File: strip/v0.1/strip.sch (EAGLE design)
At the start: 100 parts, among them IC1 LP2992, IC11 AP1115BY50, IC2 ADP3110A-SO8, IC3 STM32-M-48, IC4 OPA335, IC5 ADP3110A-SO8, IC6 ADP3110A-SO8, Q1 IRF7828, Q2 IRF7828, Q3 IRF7828, Q4 IRF7828, Q5 IRF7828, Q6 IRF7828

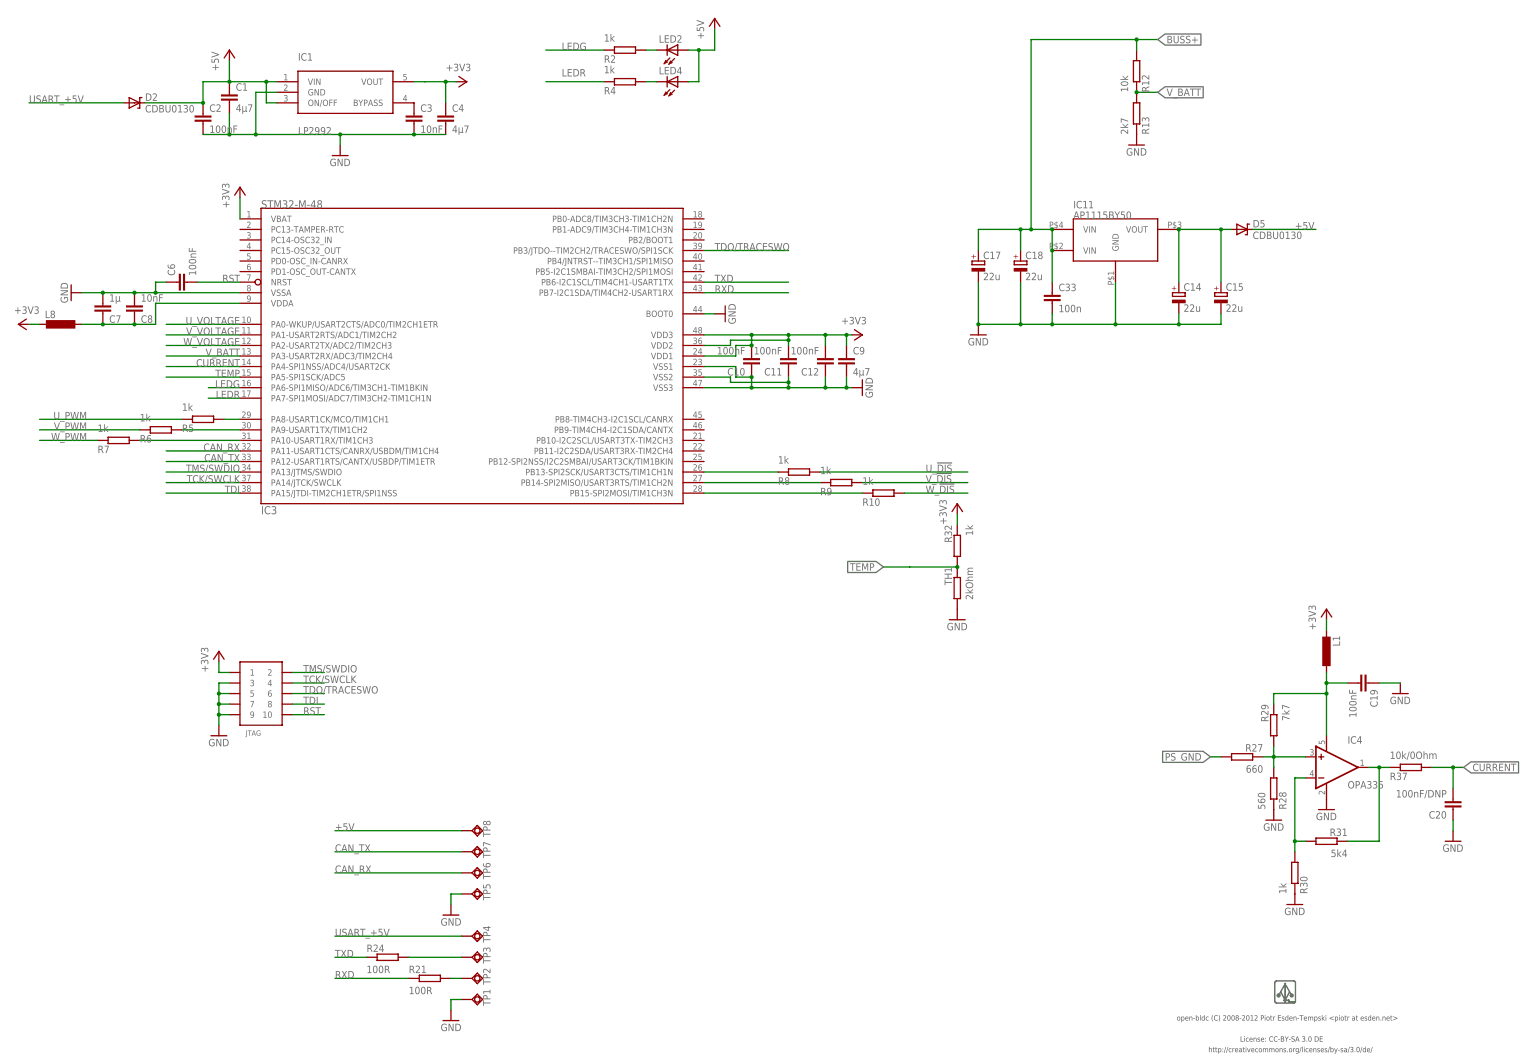
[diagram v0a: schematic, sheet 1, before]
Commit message: More work on strip. Preliminary routing of the power stage.
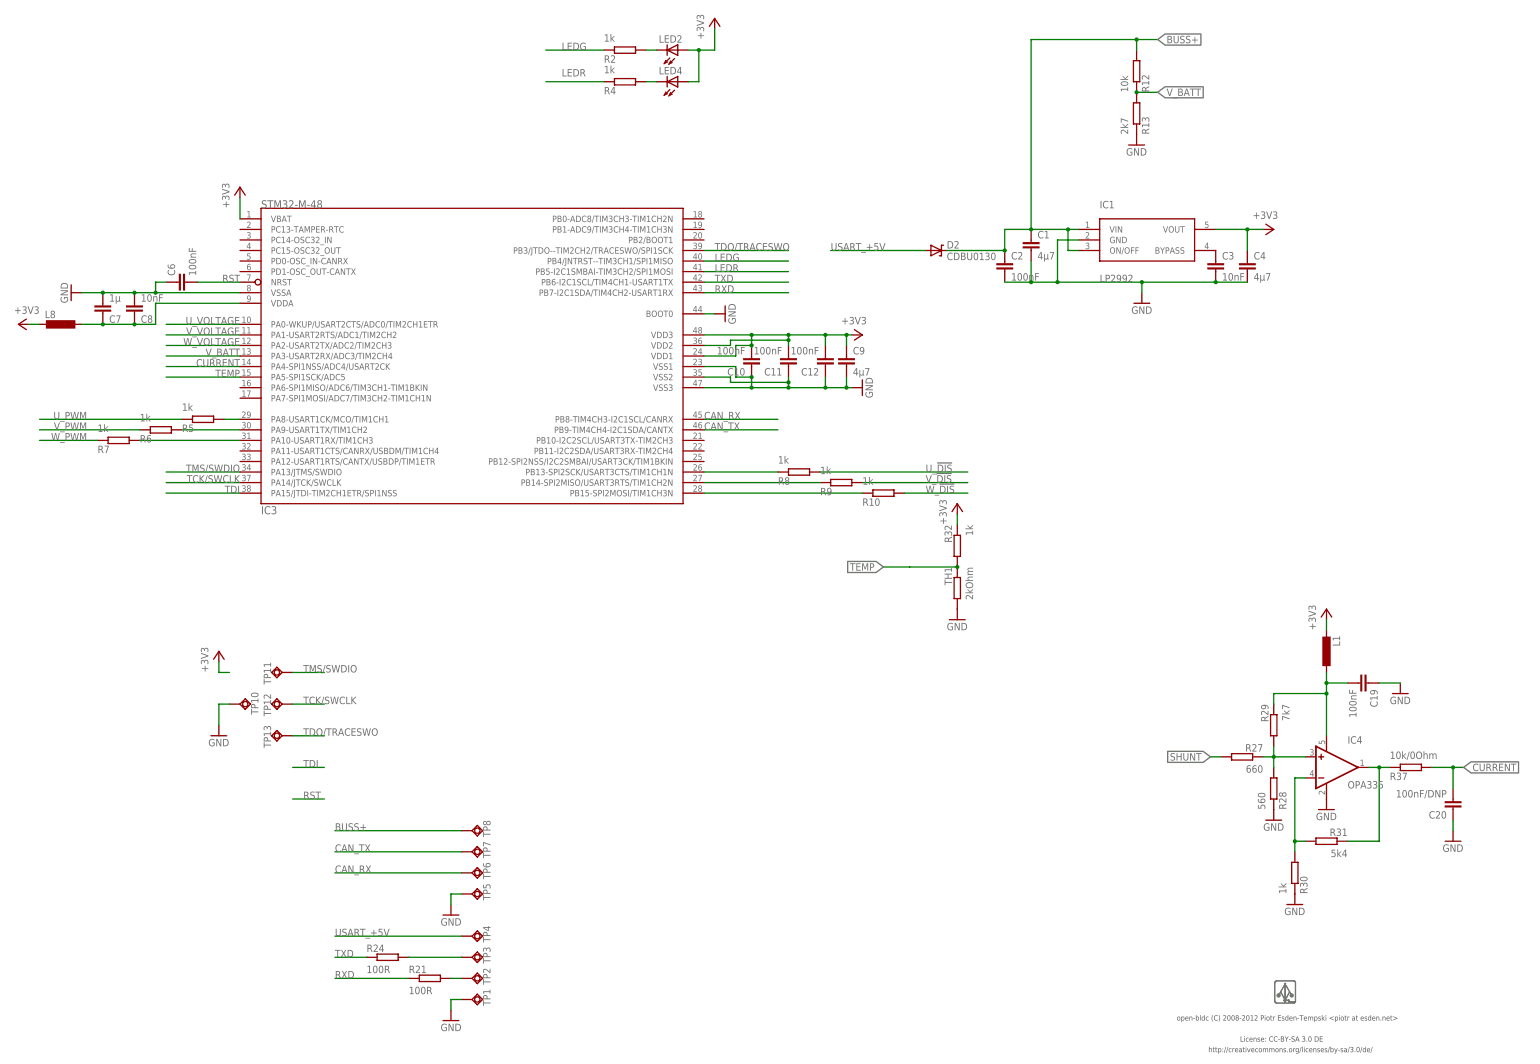
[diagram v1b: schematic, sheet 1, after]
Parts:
- removed C14, C15, C17, C18: 22u, pel_dipol_comp:CAPACITOR-POL-0805
- removed C33: 100n, pel_dipol_comp:CAPACITOR-0402
- removed D5: CDBU0130, pel_dipol_comp:DIODE-ZENER-0603
- removed IC11: AP1115BY50, clogic-v0_3-r1:AP1115BY50
- removed JTAG: CONN_5-2-FTSH-V, pel_misc:CONN_5-2-FTSH-V
- added TP10, TP11, TP12, TP13: TPSQTP11SQ, testpad:TPSQTP11SQ
- C11: device pel_dipol_comp:CAPACITOR-0603 -> pel_dipol_comp:CAPACITOR-0402
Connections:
- removed net +5V: C1.1, C2.1, D2.C, D5.C, IC1.ON/OFF, IC1.VIN, LED2.A, LED4.A, TP8.TP
- removed net +5VOUT: C14.+, C15.+, D5.A, IC11.VOUT
- removed net PS_GND: IC2.PGND, IC5.PGND, IC6.PGND, Q2.S1, Q2.S2, Q2.S3, Q4.S1, Q4.S2, Q4.S3, Q6.S1, Q6.S2, Q6.S3, R27.2, R45.1
- new net SHUNT: PAD4.P, R27.2, R45.2
- net +3V3: now also LED2.A, LED4.A; no longer JTAG.1
- net BUSS+: now also C1.1, C2.1, D2.C, IC1.ON/OFF, IC1.VIN, TP8.TP; no longer C17.+, C18.+, C33.1, IC11.VIN, IC11.VIN@2
- net CAN_RX: now also IC3.PB8-TIM4CH3-I2C1SCL/CANRX; no longer IC3.PA11-USART1CTS/CANRX/USBDM/TIM1CH4
- net CAN_TX: now also IC3.PB9-TIM4CH4-I2C1SDA/CANTX; no longer IC3.PA12-USART1RTS/CANTX/USBDP/TIM1ETR
- net GND: now also IC2.PGND, IC5.PGND, IC6.PGND, Q2.S1, Q2.S2, Q2.S3, Q4.S1, Q4.S2, Q4.S3, Q6.S1, Q6.S2, Q6.S3, R45.1, TP10.TP; no longer C14.-, C15.-, C17.-, C18.-, C33.2, IC11.GND, JTAG.3, JTAG.5, JTAG.7, JTAG.9, PAD4.P, R45.2
- net LEDG: now also IC3.PB4/JNTRST--TIM3CH1/SPI1MISO; no longer IC3.PA6-SPI1MISO/ADC6/TIM3CH1-TIM1BKIN
- net LEDR: now also IC3.PB5-I2C1SMBAI-TIM3CH2/SPI1MOSI; no longer IC3.PA7-SPI1MOSI/ADC7/TIM3CH2-TIM1CH1N
- net RST: no longer JTAG.10
- net TCK/SWCLK: now also TP12.TP; no longer JTAG.4
- net TDI: no longer JTAG.8
- net TDO/TRACESWO: now also TP13.TP; no longer JTAG.6
- net TMS/SWDIO: now also TP11.TP; no longer JTAG.2
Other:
- moved on the sheet: C1, C2, C3, C4, D2, IC1

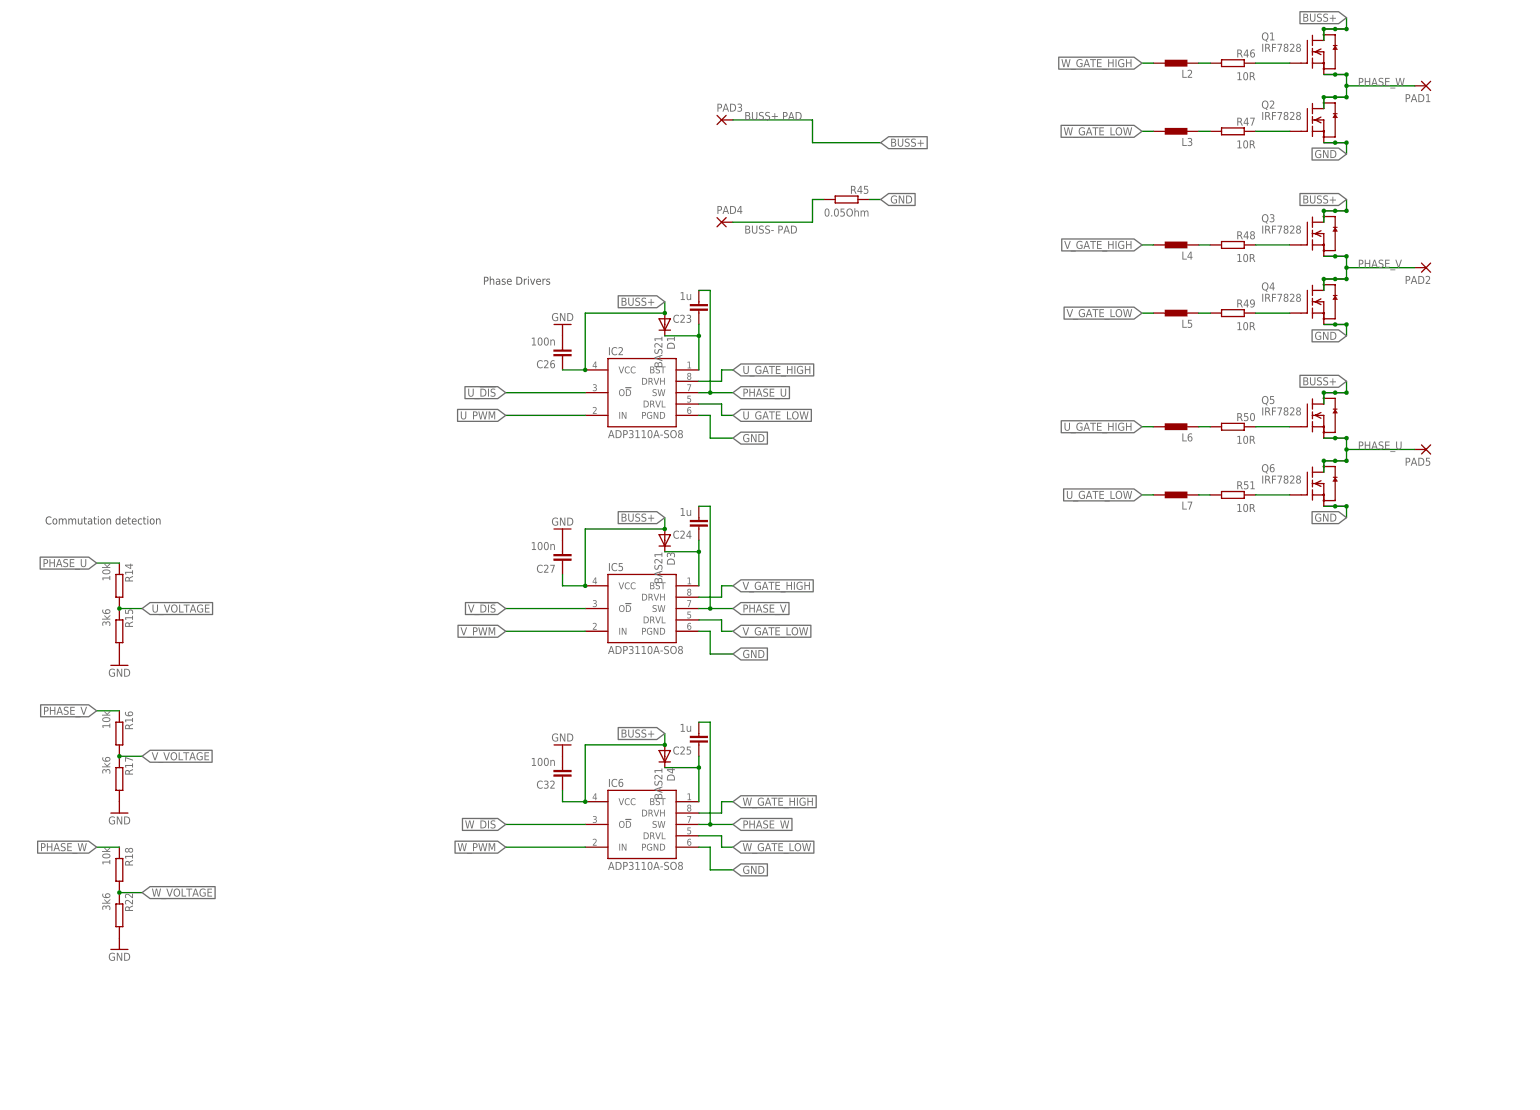
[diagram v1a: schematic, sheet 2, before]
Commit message: Logic is on real GND now not pstage GND, to prevent current related logic signal bouncing. Added mounting holes.
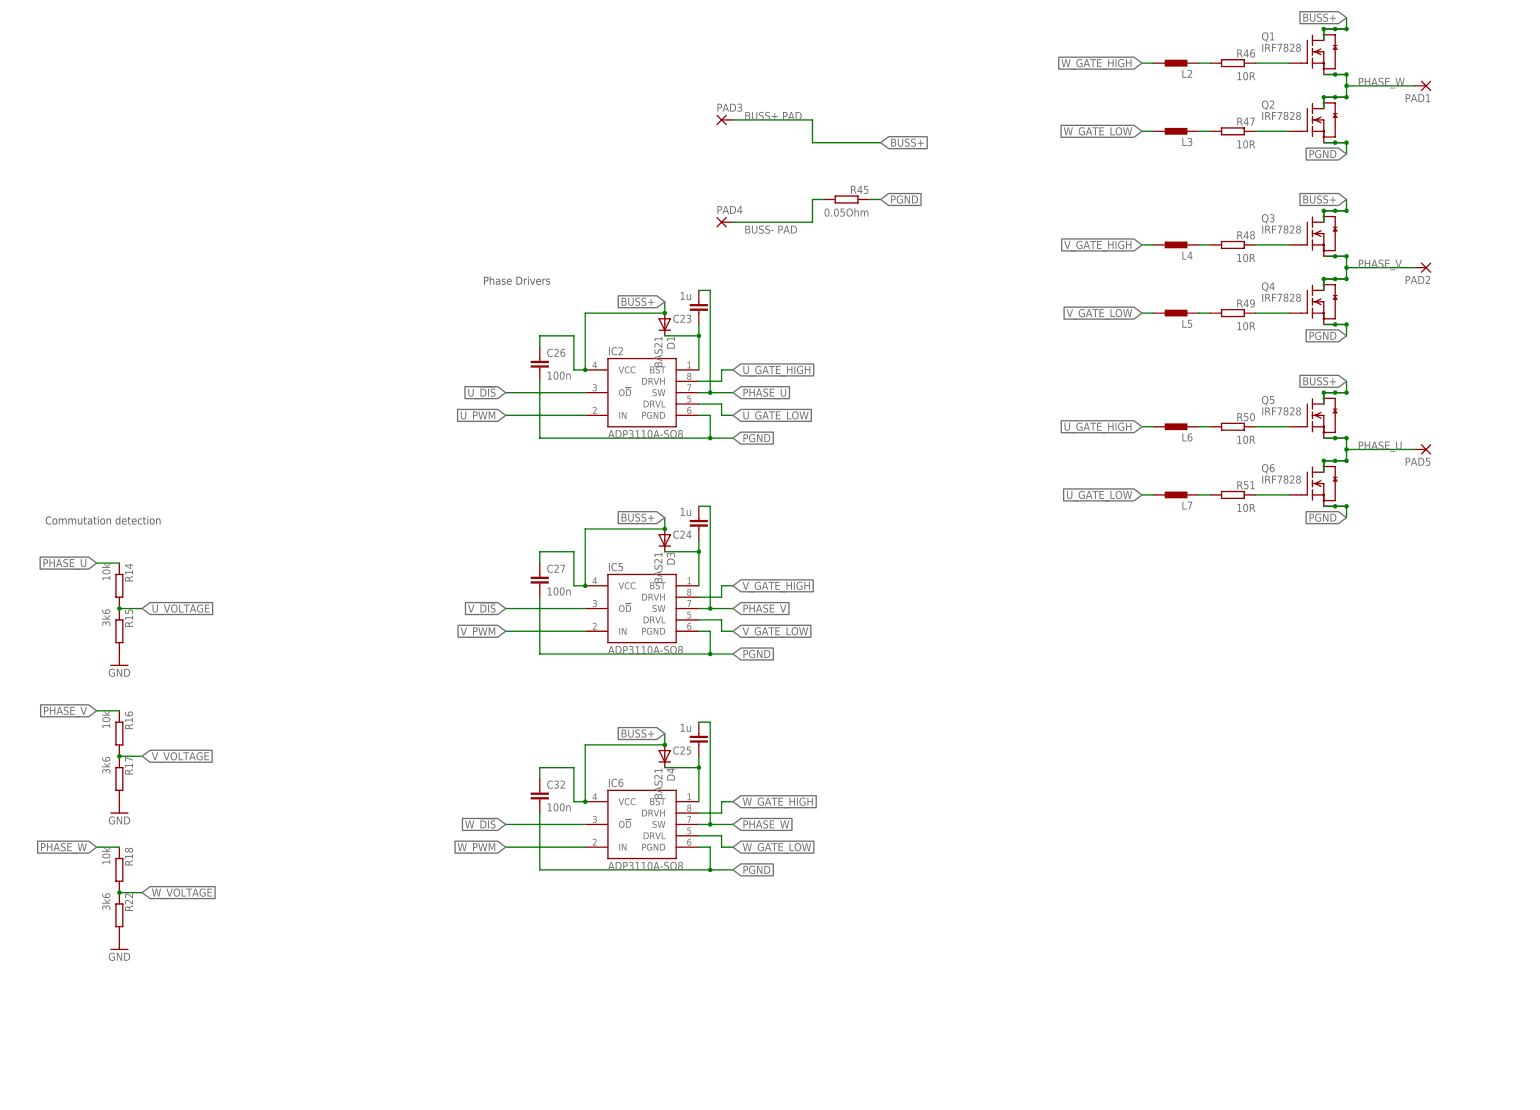
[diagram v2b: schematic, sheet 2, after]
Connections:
- removed net SHUNT: PAD4.P, R27.2, R45.2
- new net PGND: C26.2, C27.2, C32.2, IC2.PGND, IC5.PGND, IC6.PGND, Q2.S1, Q2.S2, Q2.S3, Q4.S1, Q4.S2, Q4.S3, Q6.S1, Q6.S2, Q6.S3, R27.2, R45.1
- net GND: now also PAD4.P, R45.2; no longer C26.2, C27.2, C32.2, IC2.PGND, IC5.PGND, IC6.PGND, Q2.S1, Q2.S2, Q2.S3, Q4.S1, Q4.S2, Q4.S3, Q6.S1, Q6.S2, Q6.S3, R45.1
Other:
- moved on the sheet: C26, C27, C32

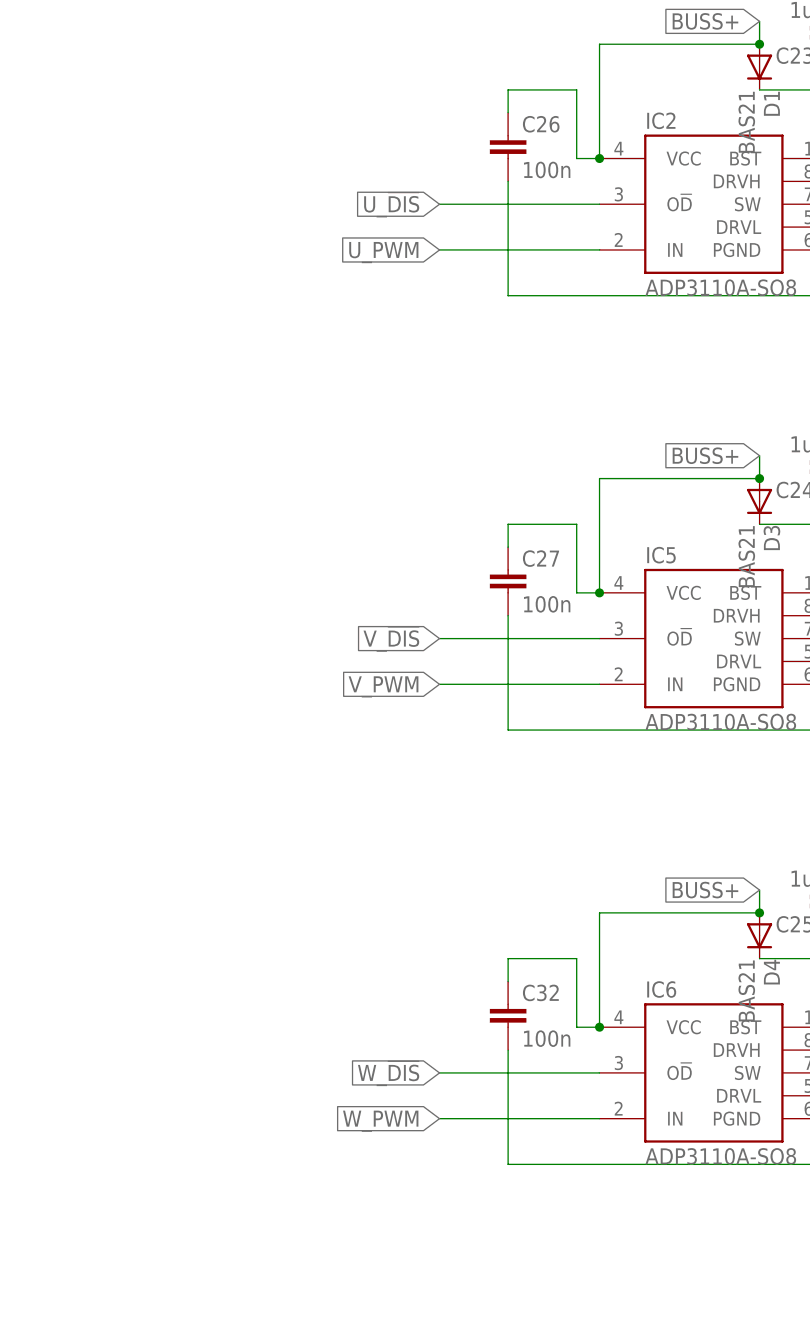
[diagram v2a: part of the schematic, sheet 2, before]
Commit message: Some more routing on strip. Connected all the control and feedback signals from the powerstage to the MCU.
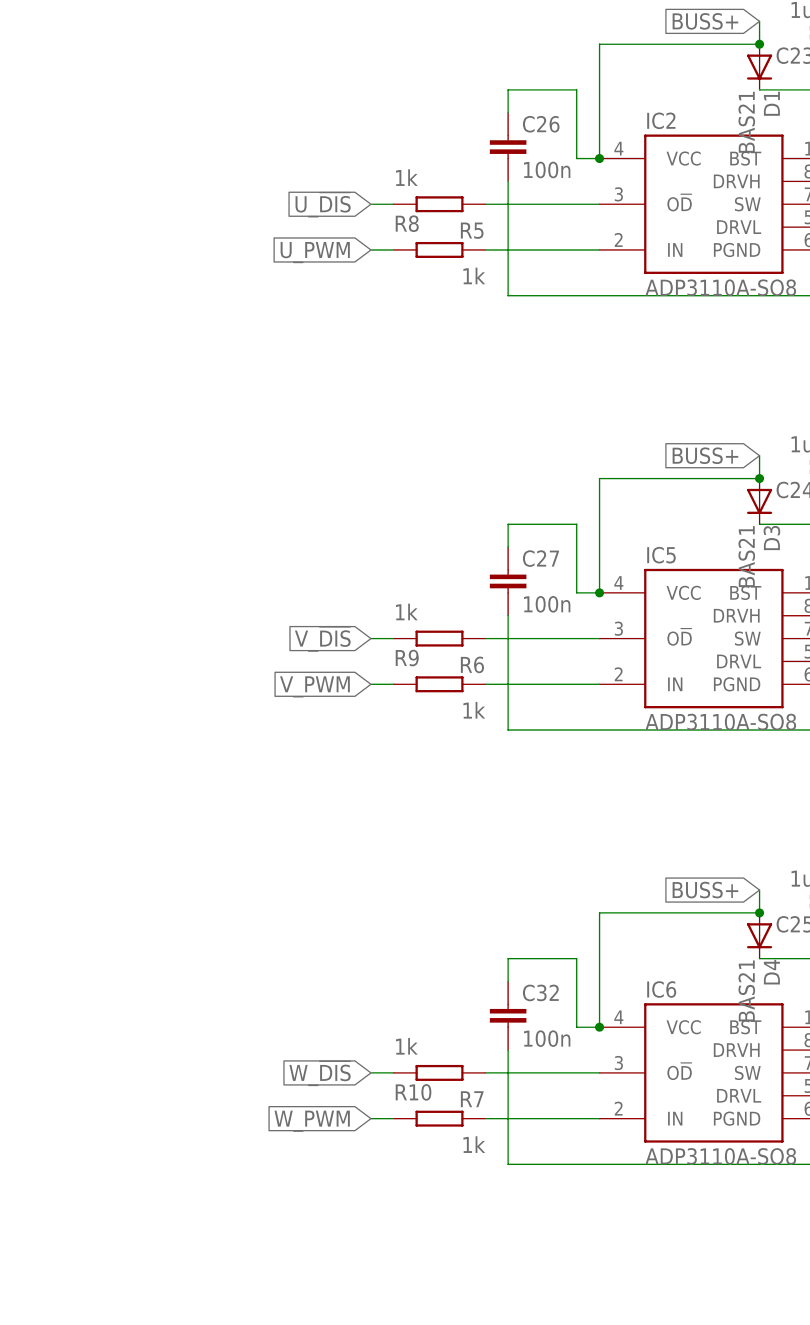
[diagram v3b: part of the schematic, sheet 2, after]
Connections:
- removed net N$33: IC3.PB13-SPI2SCK/USART3CTS/TIM1CH1N, R8.1
- removed net N$36: IC3.PB14-SPI2MISO/USART3RTS/TIM1CH2N, R9.1
- removed net N$39: IC3.PB15-SPI2MOSI/TIM1CH3N, R10.1
- removed net N$41: IC3.PA8-USART1CK/MCO/TIM1CH1, R5.2
- removed net N$42: IC3.PA9-USART1TX/TIM1CH2, R6.2
- removed net N$45: IC3.PA10-USART1RX/TIM1CH3, R7.2
- new net U_!DIS!1: IC2.O!D, R8.2
- new net U_PWM1: IC2.IN, R5.1
- new net V_!DIS!1: IC5.O!D, R9.2
- new net V_PWM1: IC5.IN, R6.1
- new net W_!DIS1: IC6.O!D, R10.2
- new net W_PWM1: IC6.IN, R7.1
- net U_!DIS: now also IC3.PB13-SPI2SCK/USART3CTS/TIM1CH1N, R8.1; no longer IC2.O!D, R8.2
- net U_PWM: now also IC3.PA8-USART1CK/MCO/TIM1CH1, R5.2; no longer IC2.IN, R5.1
- net V_!DIS: now also IC3.PB14-SPI2MISO/USART3RTS/TIM1CH2N, R9.1; no longer IC5.O!D, R9.2
- net V_PWM: now also IC3.PA9-USART1TX/TIM1CH2, R6.2; no longer IC5.IN, R6.1
- net W_!DIS: now also IC3.PB15-SPI2MOSI/TIM1CH3N, R10.1; no longer IC6.O!D, R10.2
- net W_PWM: now also IC3.PA10-USART1RX/TIM1CH3, R7.2; no longer IC6.IN, R7.1
